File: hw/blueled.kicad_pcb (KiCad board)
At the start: 2 copper layers, 33 x 63.5 mm, 29 parts, among them J1 Barrel_Jack, J2 LED Strip, J3 ICSP, Q1 Q_PMOS_SDG, Q2 Q_PNP_EBC, SW2 PUSH, U1 ATmega328P-AU, U2 HC-05, U3 AMS1117-3.3, U4 AT25SF081, X1 RESON-MURATA-CSTCE

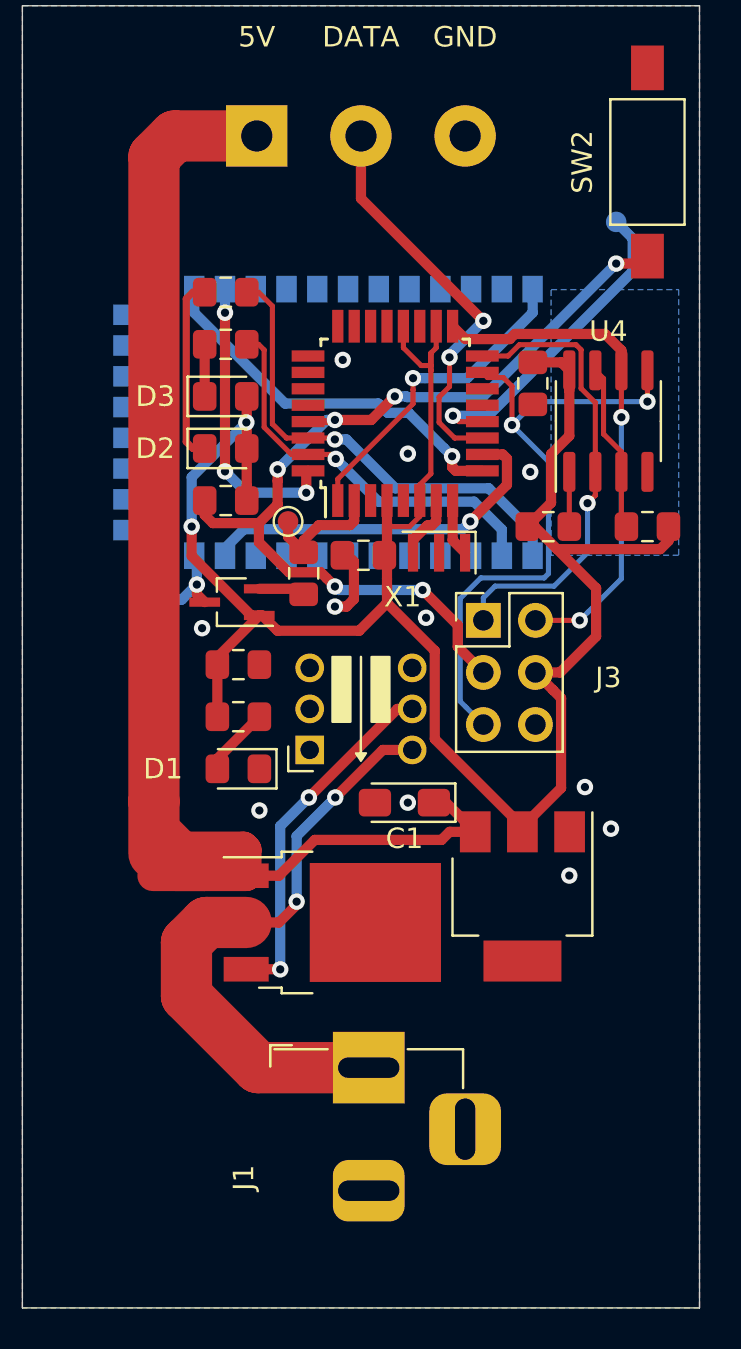
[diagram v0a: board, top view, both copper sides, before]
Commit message: fix: move tantalum capacitor from switch
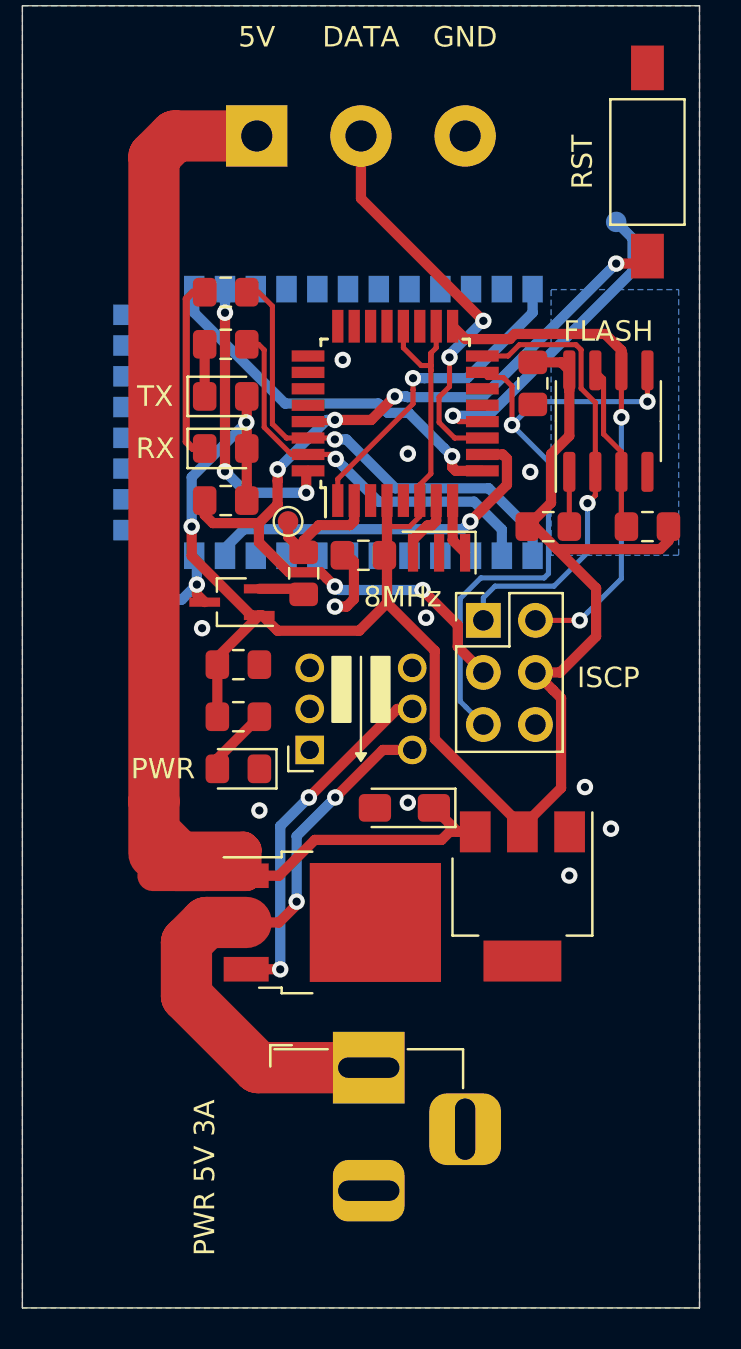
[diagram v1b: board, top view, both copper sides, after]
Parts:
- PWR 5V 3A: renamed from J1
- moved C1 0.25 mm to (157.4, 114.0)
- renumbered X1 to 8MHz, U4 to FLASH, DBG1 to HC-PWR, J3 to ISCP, DBG0 to PB0, D1 to PWR, SW2 to RST, D2 to RX, D3 to TX
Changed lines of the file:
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@@
   )
   (setup
-    (last_trace_width 0.25)
+    (last_trace_width 0.5)
     (user_trace_width 0.35)
     (user_trace_width 0.5)
@@
   )
   (module Capacitor_Tantalum_SMD:CP_EIA-3216-18_Kemet-A_Pad1.58x1.35mm_HandSolder (layer F.Cu)
-    (at 157.4395 113.792 180)
+    (at 157.4395 114.046 180)
     (descr "Tantalum Capacitor SMD Kemet-A (3216-18 Metric), IPC_7351 nominal, (Body size from: http://www.kemet.com/Lists/ProductCatalog/Attachments/253/KEM_TC101_STD.pdf), generated with kicad-footprint-generator")
     (tags "capacitor tantalum")
     (attr smd)
-    (fp_text reference C1 (at 0 -1.75) (layer F.SilkS)
+    (fp_text reference C1 (at 0 -1.75) (layer F.SilkS) hide
       (effects (font (size 1 1) (thickness 0.15)))
     )
@@
     (tags "test point SMD pad")
     (attr virtual)
-    (fp_text reference DBG1 (at 1.524 -4.572 270) (layer B.SilkS)
+    (fp_text reference HC-PWR (at 1.524 -2.286 270) (layer B.SilkS)
       (effects (font (size 1 1) (thickness 0.15)) (justify mirror))
     )
@@
     (tags "test point SMD pad")
     (attr virtual)
-    (fp_text reference DBG0 (at -1.27 -1.651) (layer B.SilkS)
+    (fp_text reference PB0 (at -1.27 -1.651) (layer B.SilkS)
       (effects (font (size 1 1) (thickness 0.15)) (justify mirror))
     )
@@
     (descr "DC Barrel Jack")
     (tags "Power Jack")
-    (fp_text reference J1 (at -5.365 -6.095 90) (layer F.SilkS)
+    (fp_text reference "PWR 5V 3A" (at -5.365 -8 90) (layer F.SilkS)
       (effects (font (size 1 1) (thickness 0.15)))
     )
@@
   (module blueled:Resonator_SMD_muRata_CSTNE_3Pin_3.2x1.3mm (layer F.Cu)
     (at 159.131 101.6 180)
-    (fp_text reference X1 (at 1.778 -2.159) (layer F.SilkS)
+    (fp_text reference 8MHz (at 1.778 -2.159) (layer F.SilkS)
       (effects (font (size 1 1) (thickness 0.15)))
     )
@@
     (tags "SOIC SO")
     (attr smd)
-    (fp_text reference U4 (at 4.38 0 180) (layer F.SilkS)
+    (fp_text reference FLASH (at 4.38 0 180) (layer F.SilkS)
       (effects (font (size 1 1) (thickness 0.15)))
     )
@@
     (descr "Through hole straight pin header, 2x03, 2.54mm pitch, double rows")
     (tags "Through hole pin header THT 2x03 2.54mm double row")
-    (fp_text reference J3 (at 6.096 2.794) (layer F.SilkS)
+    (fp_text reference ISCP (at 6.096 2.794) (layer F.SilkS)
       (effects (font (size 1 1) (thickness 0.15)))
     )
@@
     (tags "LED handsolder")
     (attr smd)
-    (fp_text reference D3 (at -3.438 0) (layer F.SilkS)
+    (fp_text reference TX (at -3.438 0) (layer F.SilkS)
       (effects (font (size 1 1) (thickness 0.15)))
     )
@@
     (tags "LED handsolder")
     (attr smd)
-    (fp_text reference D2 (at -3.438 0) (layer F.SilkS)
+    (fp_text reference RX (at -3.438 0) (layer F.SilkS)
       (effects (font (size 1 1) (thickness 0.15)))
     )
@@
     (tags "LED handsolder")
     (attr smd)
-    (fp_text reference D1 (at 3.674 0) (layer F.SilkS)
+    (fp_text reference PWR (at 3.674 0) (layer F.SilkS)
       (effects (font (size 1 1) (thickness 0.15)))
     )
@@
     (tags "SPST button tactile switch")
     (attr smd)
-    (fp_text reference SW2 (at 0 -3.175 90) (layer F.SilkS)
+    (fp_text reference RST (at 0 -3.175 90) (layer F.SilkS)
       (effects (font (size 1 1) (thickness 0.15)))
     )
@@
   (segment (start 145.225981 116.269981) (end 146.31 117.354) (width 1.5) (layer F.Cu) (net 39))
   (segment (start 147.707 117.354) (end 146.31 117.354) (width 1.5) (layer F.Cu) (net 39))
-  (segment (start 159.250999 115.608001) (end 159.645 115.214) (width 0.5) (layer F.Cu) (net 39))
-  (segment (start 159.645 115.214) (end 160.895 115.214) (width 0.5) (layer F.Cu) (net 39))
   (segment (start 153.069999 115.608001) (end 159.250999 115.608001) (width 0.5) (layer F.Cu) (net 39))
   (segment (start 151.324 117.354) (end 153.069999 115.608001) (width 0.5) (layer F.Cu) (net 39))
   (segment (start 149.724 117.354) (end 151.324 117.354) (width 0.5) (layer F.Cu) (net 39))
   (segment (start 147.707 117.354) (end 145.167 117.354) (width 1.5) (layer F.Cu) (net 39))
-  (segment (start 159.473 113.792) (end 160.895 115.214) (width 0.5) (layer F.Cu) (net 39))
-  (segment (start 158.877 113.792) (end 159.473 113.792) (width 0.5) (layer F.Cu) (net 39))
+  (segment (start 159.645 115.214) (end 159.250999 115.608001) (width 0.5) (layer F.Cu) (net 39))
+  (segment (start 160.895 115.214) (end 159.645 115.214) (width 0.5) (layer F.Cu) (net 39))
+  (segment (start 160.045 115.214) (end 158.877 114.046) (width 0.5) (layer F.Cu) (net 39))
+  (segment (start 160.895 115.214) (end 160.045 115.214) (width 0.5) (layer F.Cu) (net 39))
   (segment (start 164.679999 108.291999) (end 163.83 107.442) (width 0.5) (layer F.Cu) (net 40))
   (segment (start 165.080001 113.078999) (end 165.080001 108.692001) (width 0.5) (layer F.Cu) (net 40))

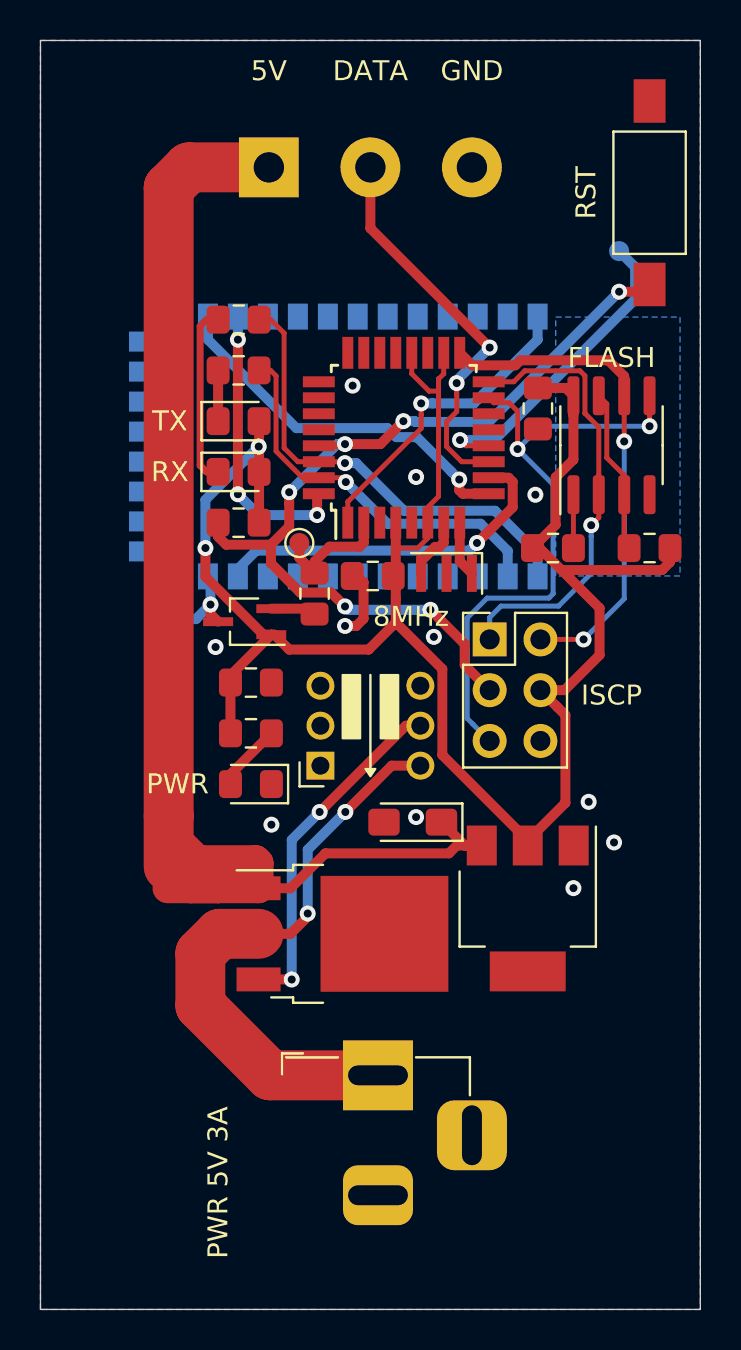
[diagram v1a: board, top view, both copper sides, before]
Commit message: fix: MOSFET pin mapping and better layouting
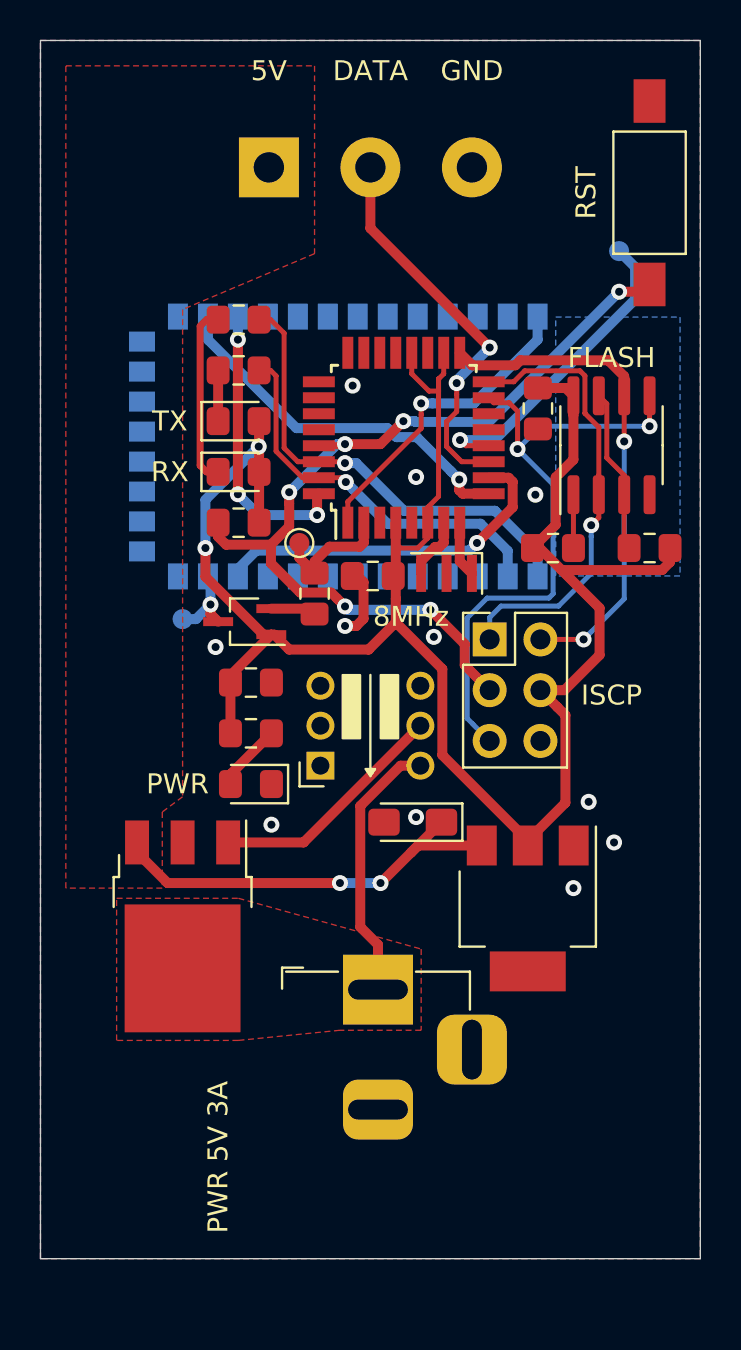
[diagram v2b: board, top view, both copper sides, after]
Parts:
- moved Q1 8.01 mm to (145.9, 119.3), turned to 270 degrees
- moved PWR 5V 3A 4.29 mm to (155.7, 122.4)
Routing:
- net /VIN: track 68.6 -> 21.3 mm, vias 0 -> 2
- net /VINJACK: track 29.8 -> 13.4 mm, vias 2 -> 0
- net Net-(Q1-Pad3): track 17.5 -> 12.0 mm, vias 2 -> 0
- added copper zone on F.Cu, net /VIN
- added copper zone on F.Cu, net /VINJACK
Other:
- board size 33 x 63.5 mm -> 33 x 61 mm

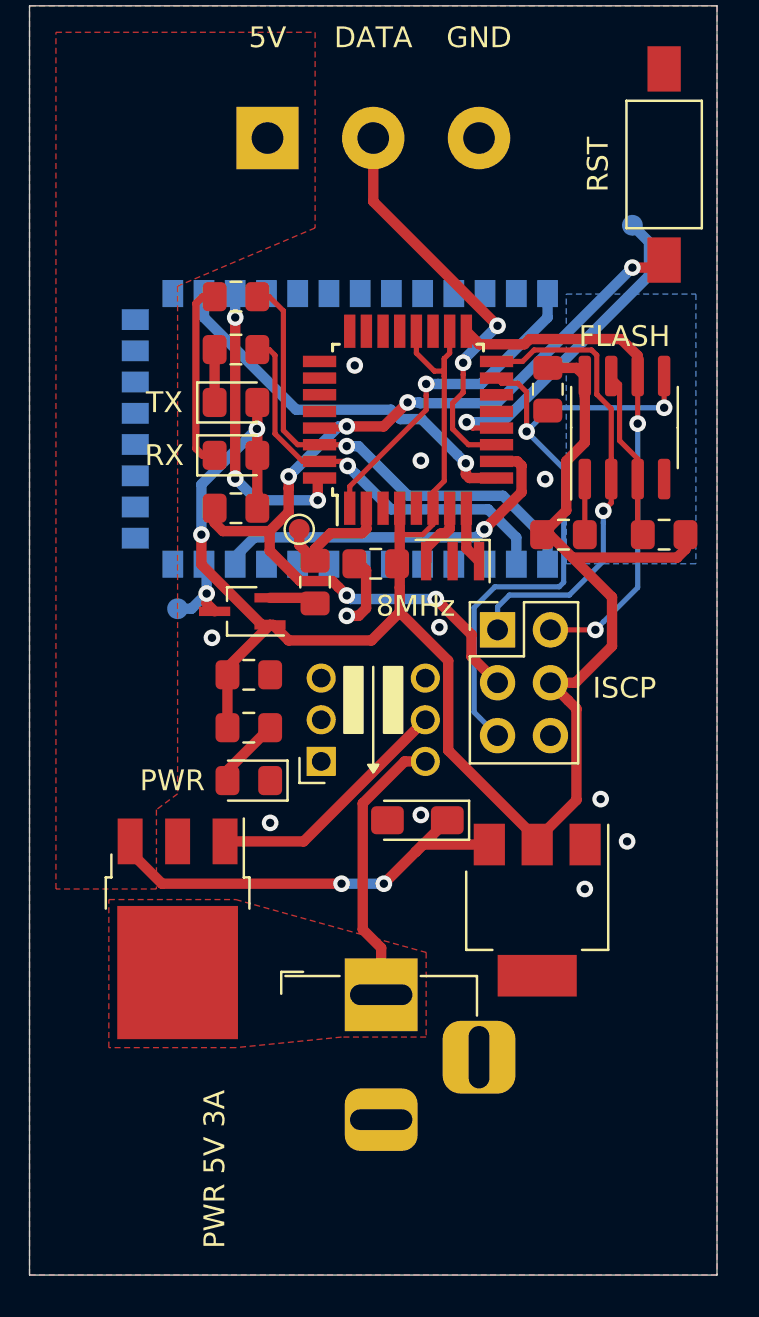
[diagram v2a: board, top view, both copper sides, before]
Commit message: add: jumpers to pcb layout
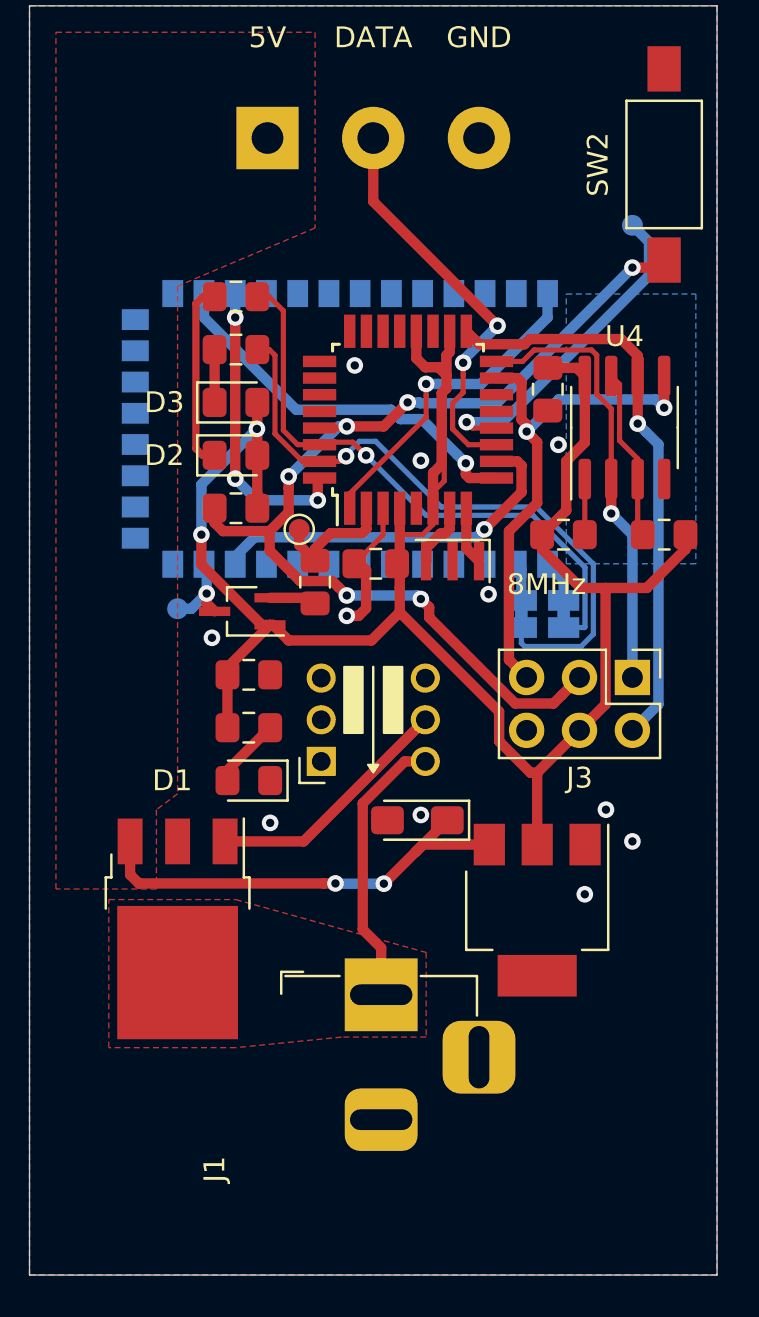
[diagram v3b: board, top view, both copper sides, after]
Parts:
- removed ISCP: ICSP, Connector_PinHeader_2.54mm:PinHeader_2x03_P2.54mm_Vertical
- added J3: ICSP, Connector_PinHeader_2.54mm:PinHeader_2x03_P2.54mm_Vertical, F.Cu at (167.8, 107.2)
- added RX: Jumper_NC_Small, Jumper:SolderJumper-2_P1.3mm_Bridged_Pad1.0x1.5mm, B.Cu at (164.5, 104.1)
- added TX: Jumper_NC_Small, Jumper:SolderJumper-2_P1.3mm_Bridged_Pad1.0x1.5mm, B.Cu at (162.4, 104.1)
- J1: renamed from PWR 5V 3A
- renumbered PWR to D1, RX to D2, TX to D3, PB0 to DBG0, HC-PWR to DBG1, RST to SW2, FLASH to U4
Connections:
- net /+3V3 renamed +3V3
- U2 pad 1: /RX -> Net-(JP1-Pad2)
- U2 pad 2: /TX -> Net-(JP2-Pad2)
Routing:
- net /TX: track 19.7 -> 31.5 mm
- net /MOSI: track 31.6 -> 25.6 mm
- net /RX: track 23.3 -> 28.5 mm
- net /RESET: track 45.4 -> 49.9 mm
- net +3V3: track 101.3 -> 104.9 mm
- net GND: track 3.53 -> 6.76 mm
- net /SCK: track 25.1 -> 27.8 mm, vias 2 -> 1
- net Net-(JP1-Pad2): track 0.00 -> 1.66 mm
- net Net-(JP2-Pad2): track 0.00 -> 1.44 mm
- net /MISO: track 22.6 -> 21.3 mm
- net /VIN: track 21.3 -> 22.0 mm
